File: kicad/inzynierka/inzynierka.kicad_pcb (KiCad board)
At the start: 2 copper layers, 170 x 175 mm, 36 parts

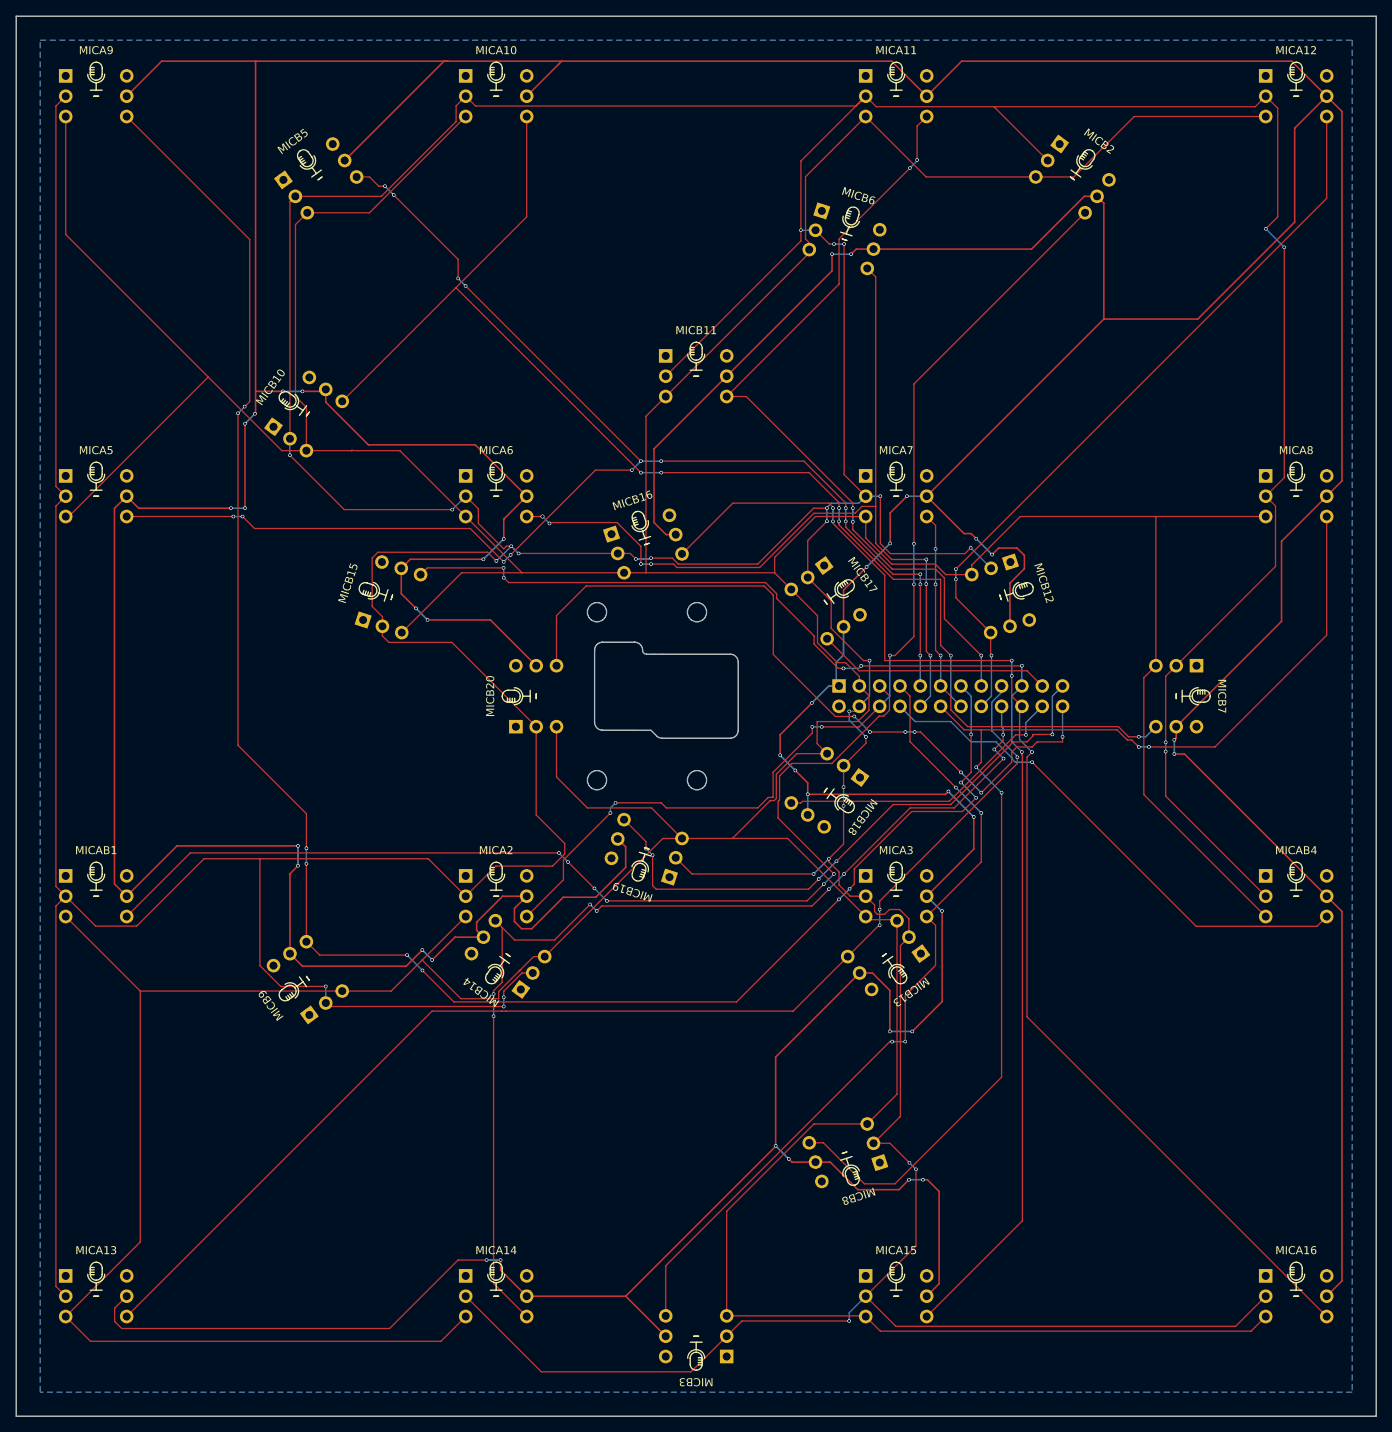
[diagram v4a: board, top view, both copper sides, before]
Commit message: Usunięcie błędów DRC dla 3.3V
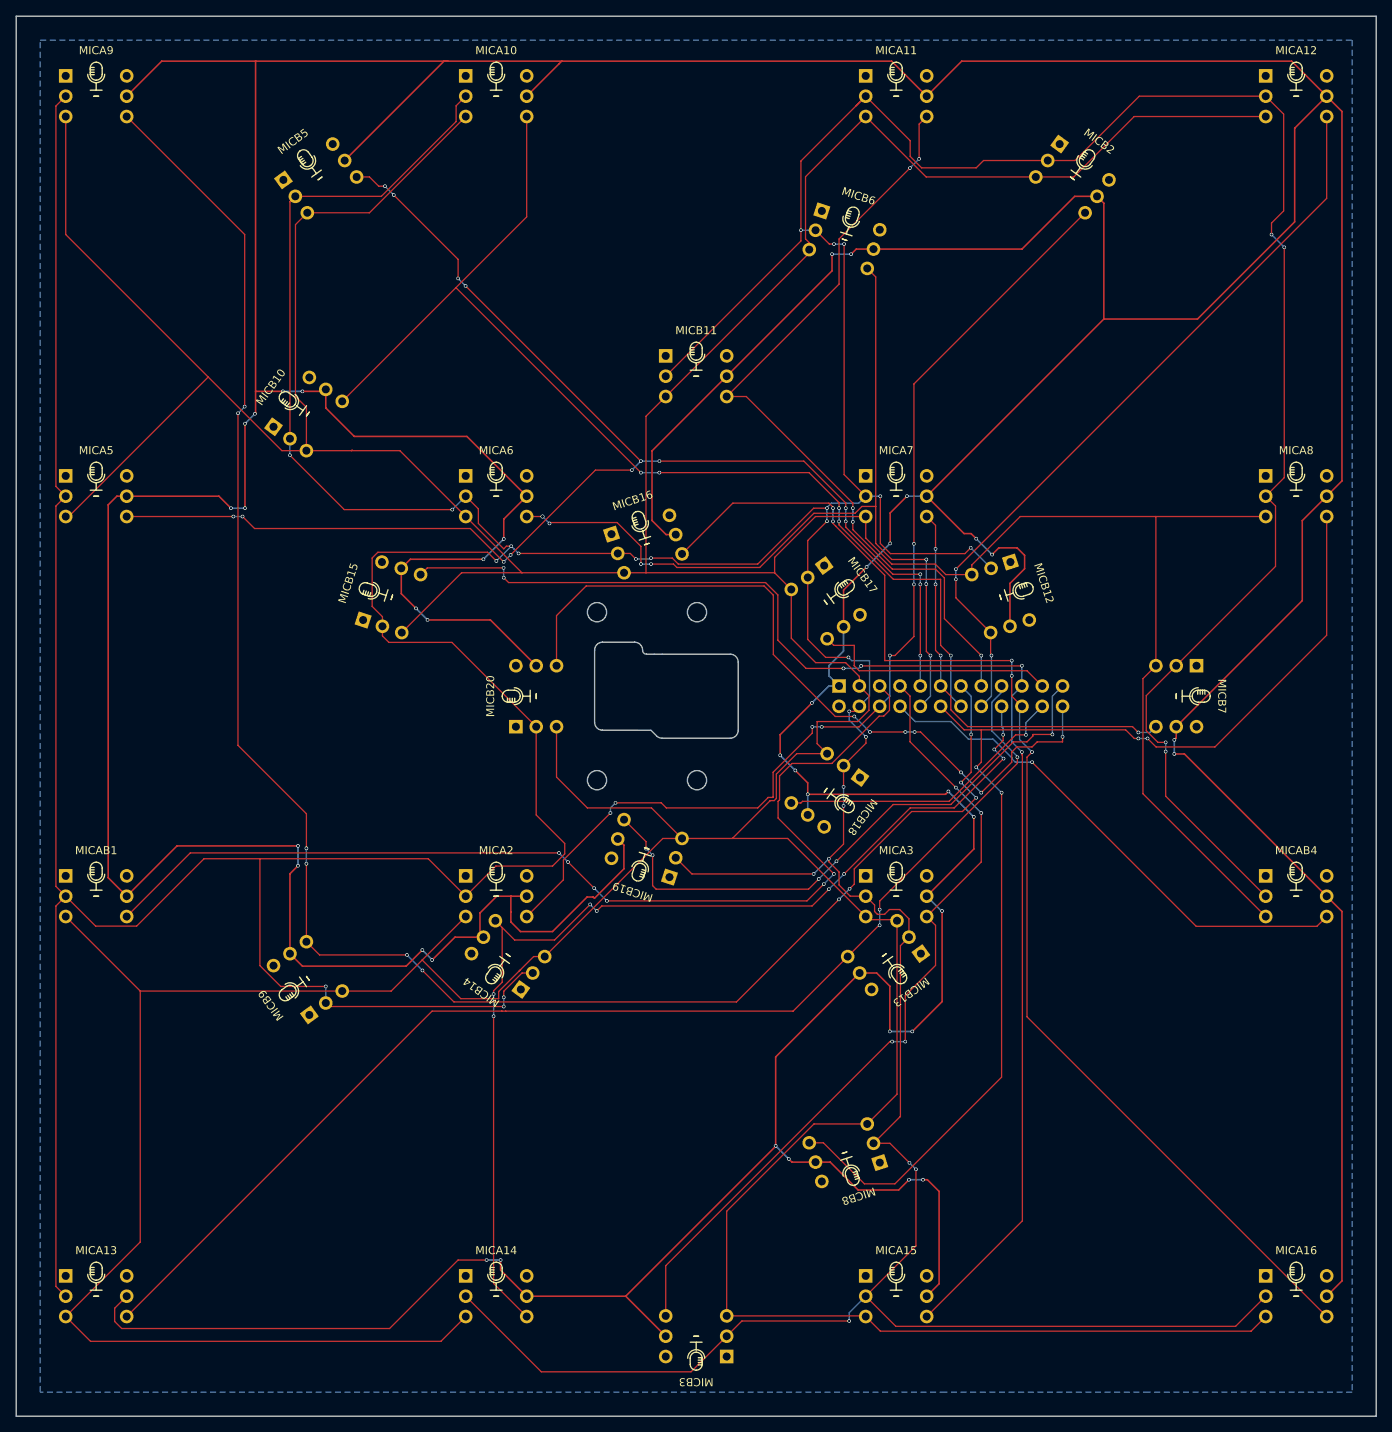
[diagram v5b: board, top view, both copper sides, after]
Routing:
- net CLK2: track 1082.1 -> 1035.9 mm
- net +3.3V: track 1149.9 -> 1153.2 mm
- net D15: track 169.9 -> 172.3 mm
- net CLK1: track 913.7 -> 915.4 mm
- net D17: track 29.3 -> 30.8 mm
- net D9: track 228.0 -> 227.5 mm

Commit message: Uładnienie połączeń
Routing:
- net CLK2: track 1035.9 -> 1045.3 mm, vias 31 -> 30
- net CLK1: track 915.4 -> 919.7 mm
- net +3.3V: track 1153.2 -> 1149.0 mm
- net D19: track 74.6 -> 78.7 mm, vias 5 -> 6
- net D20: track 93.9 -> 95.9 mm
- net D4: track 65.3 -> 66.1 mm
- net D17: track 30.8 -> 31.6 mm
- net D6: vias 8 -> 6

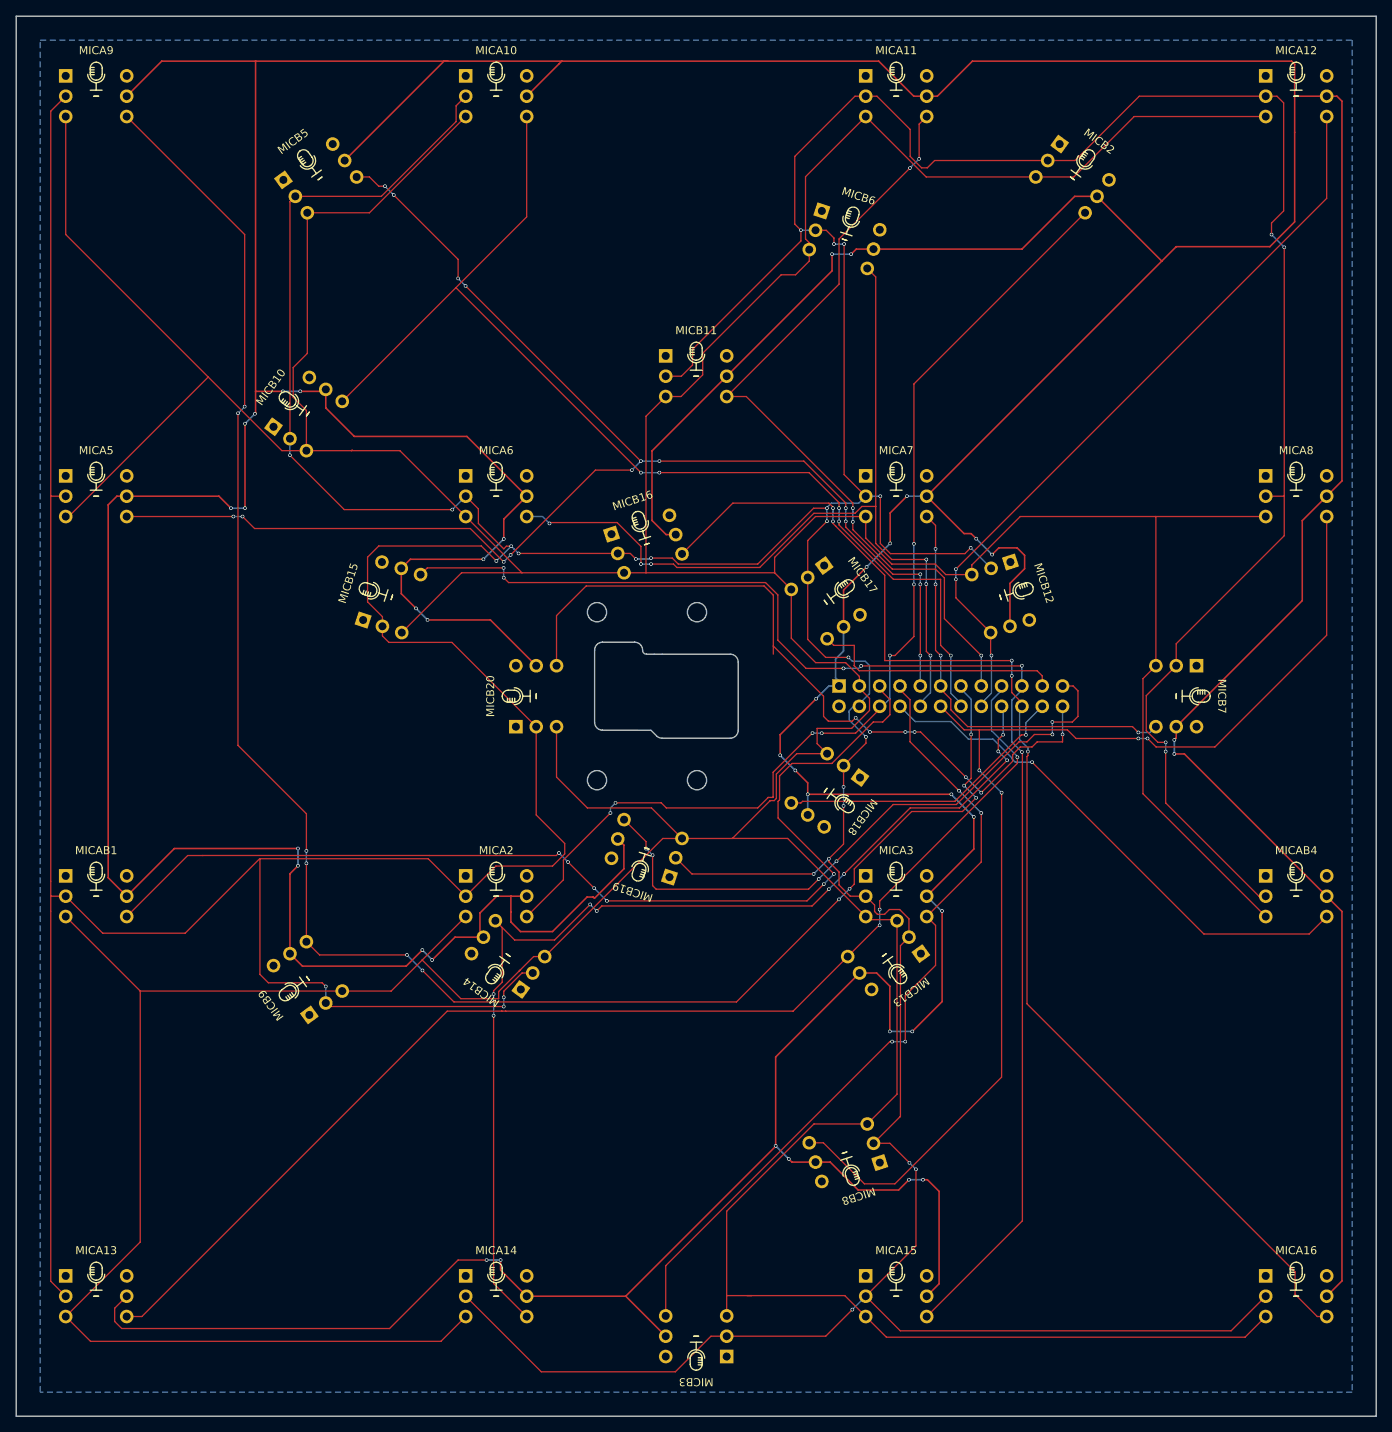
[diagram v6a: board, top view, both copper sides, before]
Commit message: Pogrubienie footprintów + poprawienie trasowania
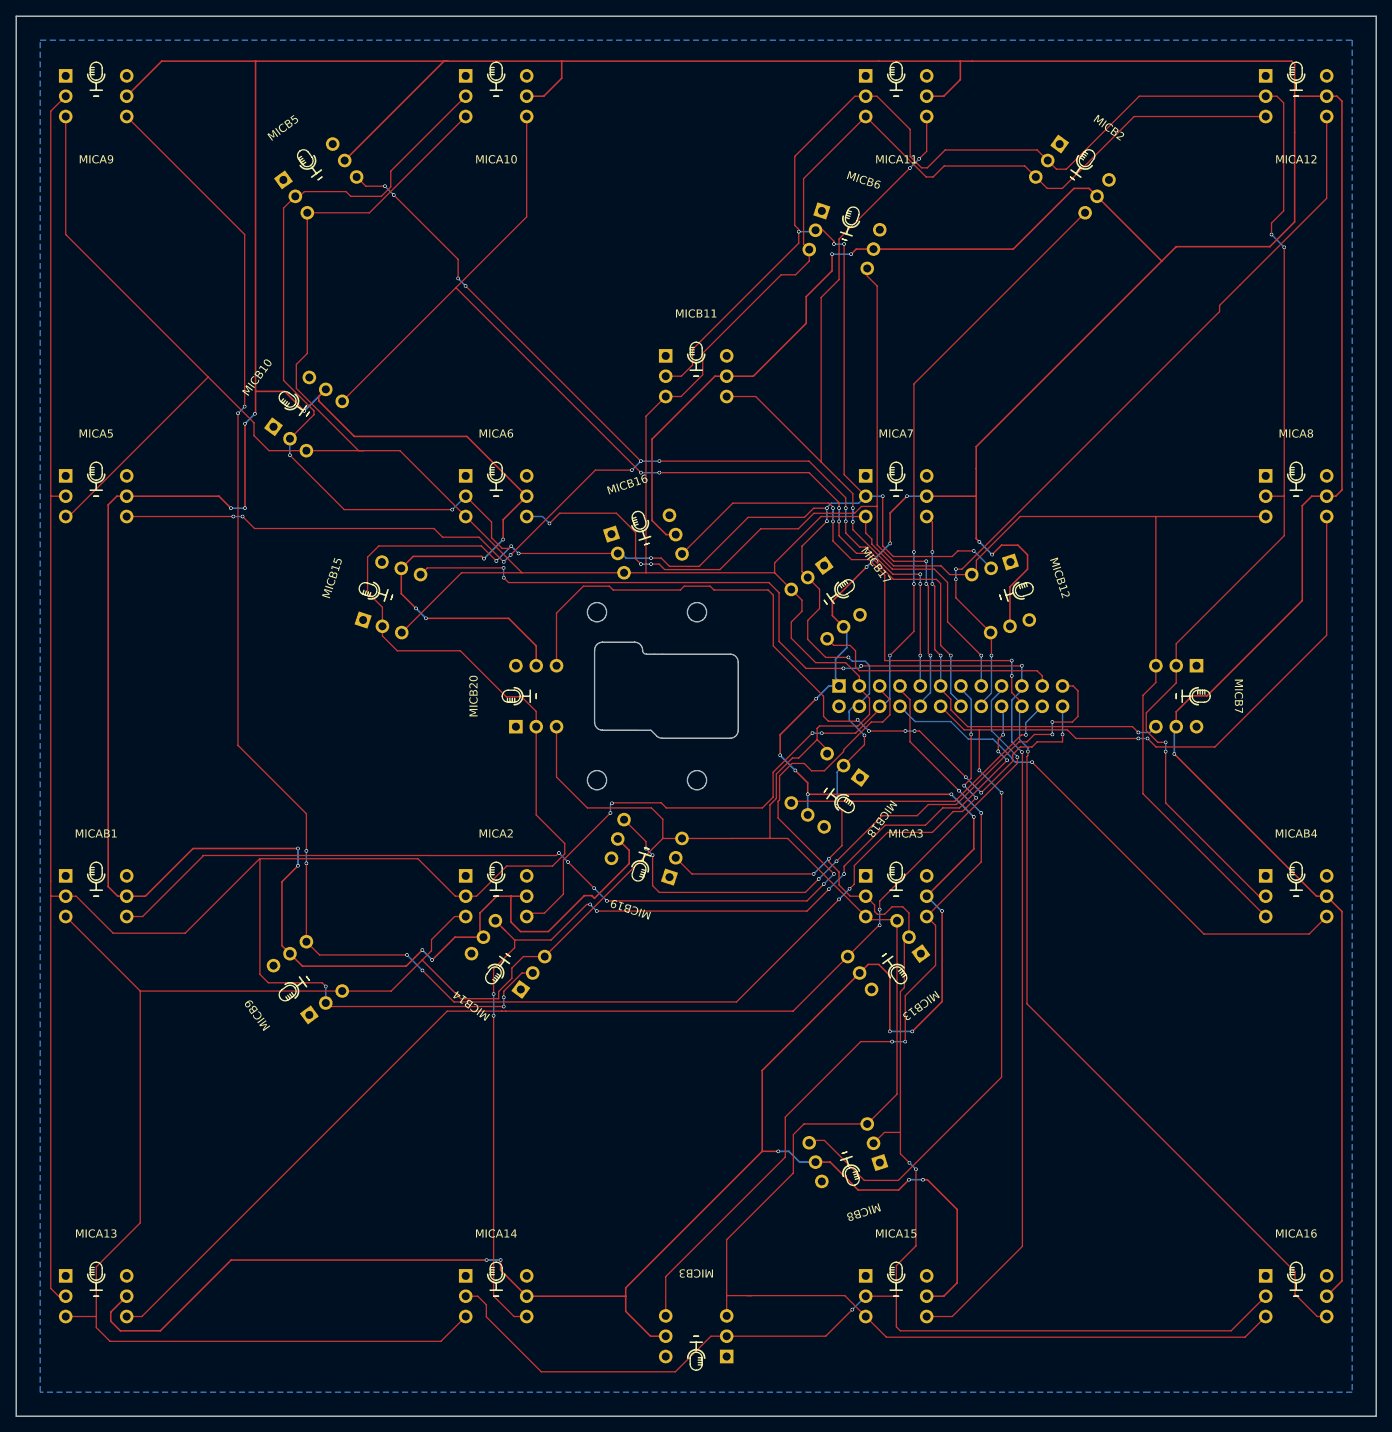
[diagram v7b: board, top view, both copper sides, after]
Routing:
- net +3.3V: track 1149.0 -> 1178.5 mm, vias 38 -> 35
- net CLK2: track 1045.3 -> 1057.2 mm, vias 30 -> 28
- net CLK1: track 919.7 -> 924.5 mm
- net D11: track 99.3 -> 103.2 mm
- net D3: track 101.3 -> 103.5 mm
- net D15: track 172.3 -> 174.4 mm
- net D6: track 112.1 -> 113.8 mm
- net D16: track 158.8 -> 160.3 mm
- net D14: track 133.3 -> 134.4 mm
- net D1: track 131.9 -> 132.9 mm
- net D2: track 132.3 -> 133.2 mm
- net D5: track 180.0 -> 180.8 mm
- net D20: track 95.9 -> 95.2 mm

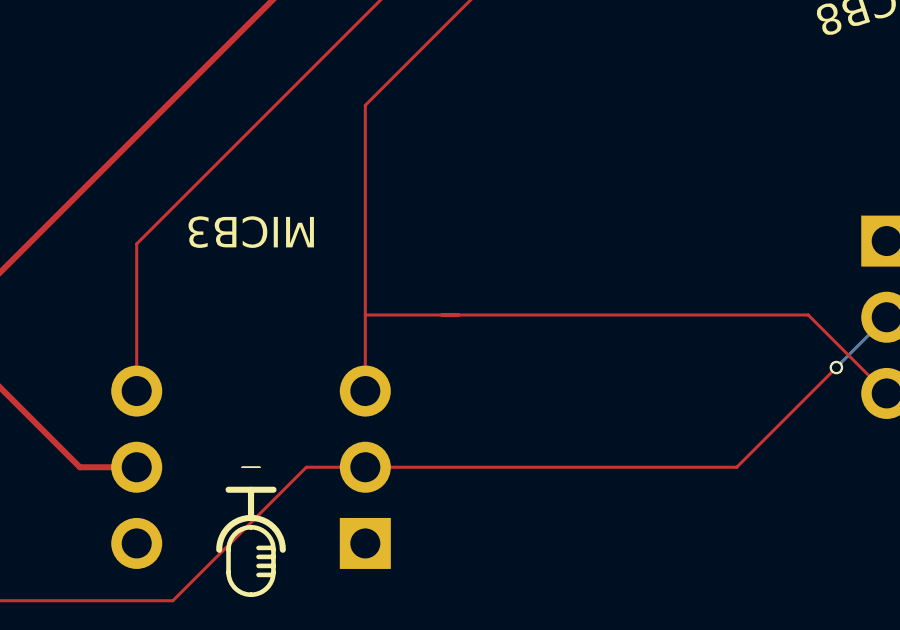
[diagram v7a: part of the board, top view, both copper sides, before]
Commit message: Poprawa łączenia termicznego dla L/R w INMP441
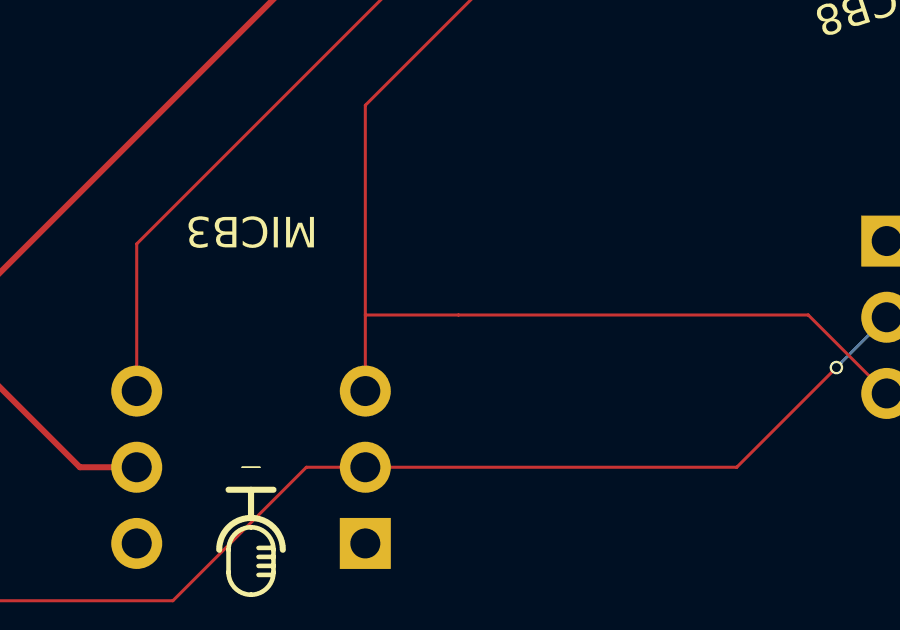
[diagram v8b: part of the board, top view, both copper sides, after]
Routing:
- net CLK1: track 924.5 -> 923.9 mm
